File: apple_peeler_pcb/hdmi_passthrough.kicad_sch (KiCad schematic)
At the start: 2 parts, among them U3 4066

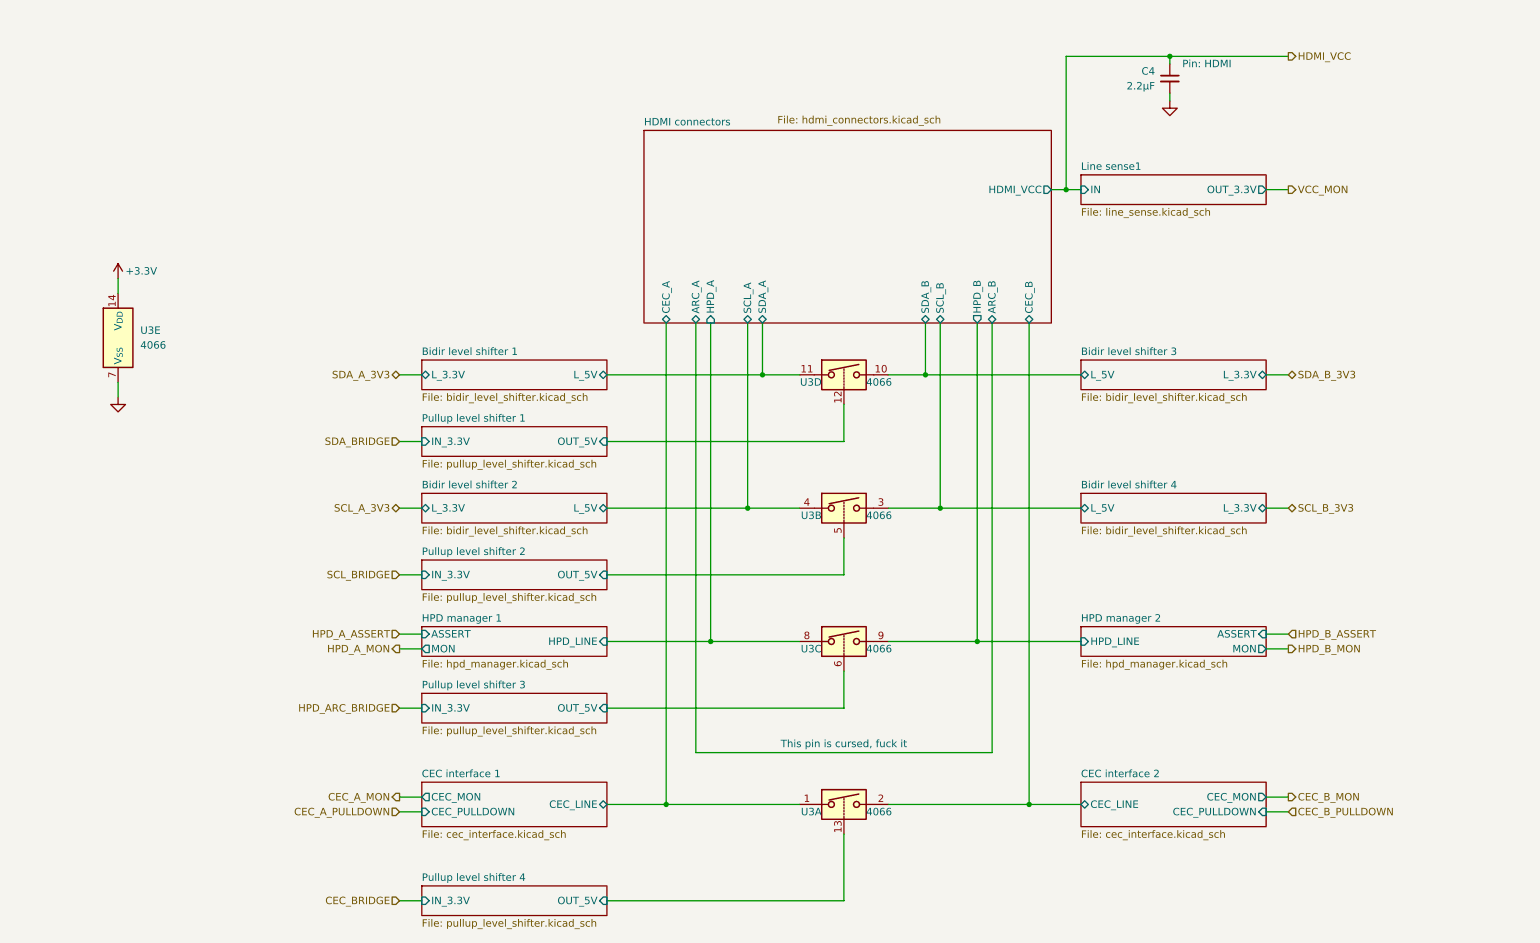
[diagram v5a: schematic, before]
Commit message: add loads of test points
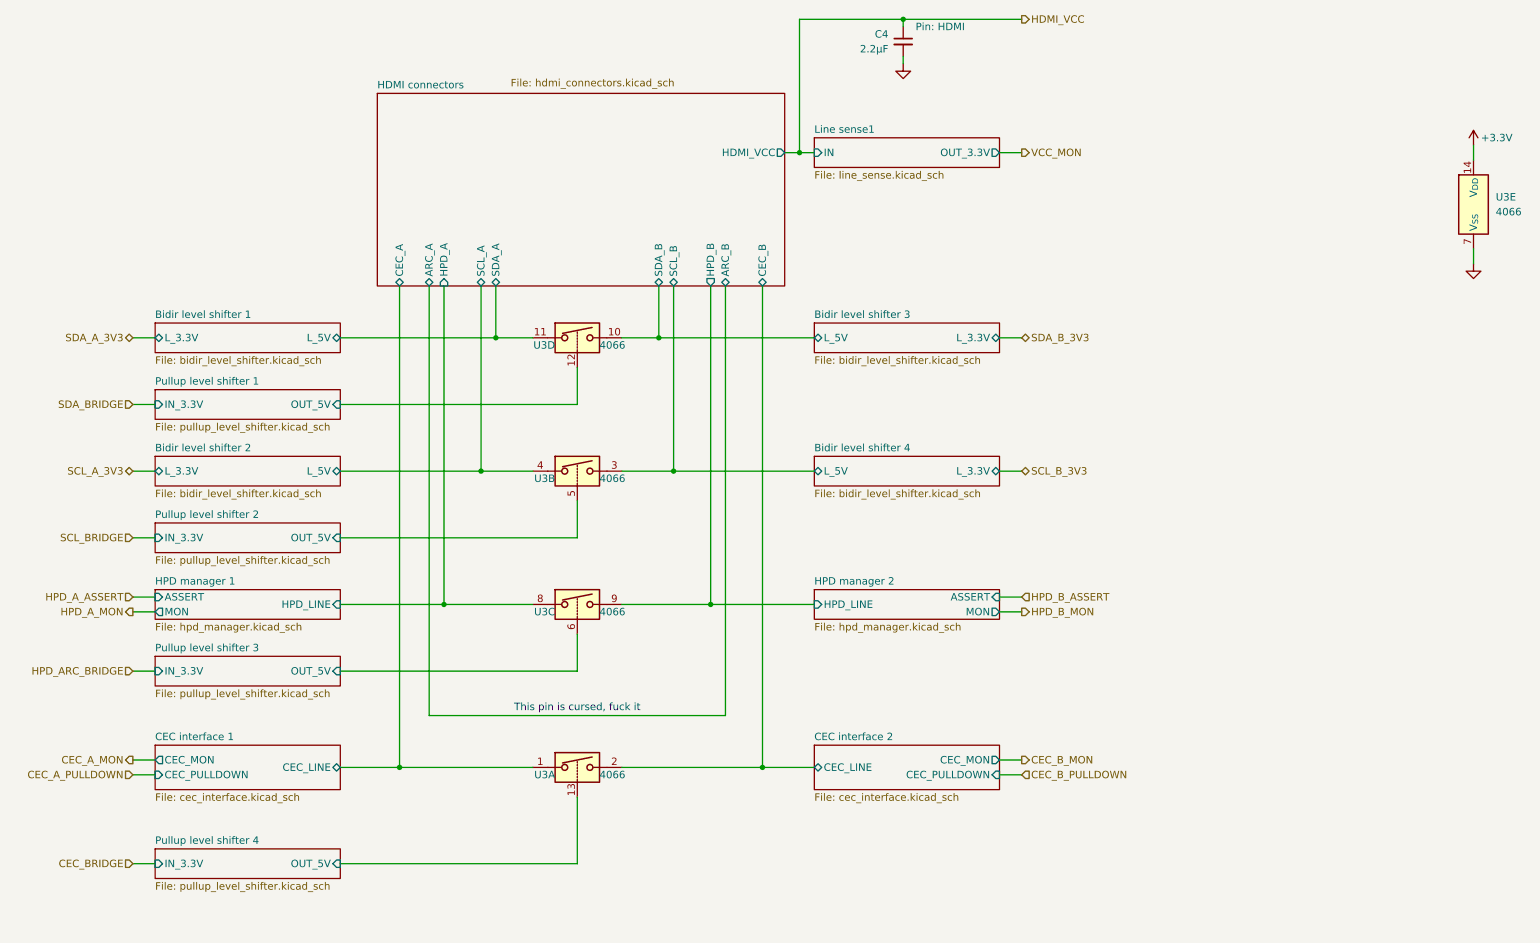
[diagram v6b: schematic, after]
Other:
- moved on the sheet: C4, U3A, U3B, U3C, U3D, U3E
